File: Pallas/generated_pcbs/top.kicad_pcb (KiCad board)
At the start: 2 copper layers, 467.5 x 140 mm, 17 parts

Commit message: Consolidate symbol and fp libraries
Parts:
- removed the MountBaseMiddleTop15 at (526.4, 136.4)
- removed the MountBaseMiddleTop15 at (526.4, 43.9)
- added MountBaseMiddleTop15: MountingHole, Pallas:MountingHole_2.2mm_M2_Pad_Via, F.Cu at (526.4, 136.4)
- added MountBaseMiddleTop15: MountingHole, Pallas:MountingHole_2.2mm_M2_Pad_Via, F.Cu at (526.4, 43.9)
- LogoBaseMiddleTop: footprint keyboard:Ciaanh_signature -> Pallas:Ciaanh_signature
- MountBaseMiddleTop0, MountBaseMiddleTop10, MountBaseMiddleTop11, MountBaseMiddleTop12, MountBaseMiddleTop13, MountBaseMiddleTop14, MountBaseMiddleTop2, MountBaseMiddleTop3, MountBaseMiddleTop4, MountBaseMiddleTop5, MountBaseMiddleTop6, MountBaseMiddleTop7, MountBaseMiddleTop8, MountBaseMiddleTop9: footprint keyboard:MountingHole_2.2mm_M2_Pad_Via -> Pallas:MountingHole_2.2mm_M2_Pad_Via
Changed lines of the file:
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@@
-(kicad_pcb (version 20171130) (host pcbnew "(5.1.4)-1")
+(kicad_pcb (version 20171130) (host pcbnew 5.1.6-c6e7f7d~86~ubuntu20.04.1)
   (general
     (thickness 1.6)
@@
     (40 Dwgs.User user)
     (41 Cmts.User user)
-    (42 Eco1.User user)
-    (43 Eco2.User user)
+    (42 Eco1.User user hide)
+    (43 Eco2.User user hide)
     (44 Edge.Cuts user)
     (45 Margin user)
@@
       (drillshape 0)
       (scaleselection 1)
-      (outputdirectory "gerber/top/"))
+      (outputdirectory "pallas/"))
   )
   (net 0 "")
@@
     (uvia_drill 0.1)
   )
-  (module keyboard:Ciaanh_signature (layer F.Cu)
+  (module Pallas:Ciaanh_signature (layer F.Cu)
     (at 72.9496 68.7784 270)
     (fp_text reference LogoBaseMiddleTop (at 0.13 6.04 270) (layer F.SilkS) hide
@@
     )
   )
-  (module keyboard:MountingHole_2.2mm_M2_Pad_Via (layer F.Cu)
+  (module Pallas:MountingHole_2.2mm_M2_Pad_Via (layer F.Cu)
     (at 368.8996 48.8784)
     (descr "Mounting Hole 2.2mm, M2")
@@
     (pad 1 thru_hole circle (at 1.166726 -1.166726) (size 0.7 0.7) (drill 0.4) (layers *.Cu *.Mask))
   )
-  (module keyboard:MountingHole_2.2mm_M2_Pad_Via (layer F.Cu)
+  (module Pallas:MountingHole_2.2mm_M2_Pad_Via (layer F.Cu)
     (at 208.8996 48.8784)
     (descr "Mounting Hole 2.2mm, M2")
@@
     (pad 1 thru_hole circle (at 1.166726 -1.166726) (size 0.7 0.7) (drill 0.4) (layers *.Cu *.Mask))
   )
-  (module keyboard:MountingHole_2.2mm_M2_Pad_Via (layer F.Cu)
+  (module Pallas:MountingHole_2.2mm_M2_Pad_Via (layer F.Cu)
     (at 421.3996 136.3784)
     (descr "Mounting Hole 2.2mm, M2")
@@
     (pad 1 thru_hole circle (at 0 0) (size 4.4 4.4) (drill 2.2) (layers *.Cu *.Mask))
   )
-  (module keyboard:MountingHole_2.2mm_M2_Pad_Via (layer F.Cu)
+  (module Pallas:MountingHole_2.2mm_M2_Pad_Via (layer F.Cu)
     (at 121.3996 136.3784)
     (descr "Mounting Hole 2.2mm, M2")
@@
     (pad 1 thru_hole circle (at 0 0) (size 4.4 4.4) (drill 2.2) (layers *.Cu *.Mask))
   )
-  (module keyboard:MountingHole_2.2mm_M2_Pad_Via (layer F.Cu)
+  (module Pallas:MountingHole_2.2mm_M2_Pad_Via (layer F.Cu)
     (at 448.918 80.1114)
     (descr "Mounting Hole 2.2mm, M2")
@@
     (pad 1 thru_hole circle (at 0 0) (size 4.4 4.4) (drill 2.2) (layers *.Cu *.Mask))
   )
-  (module keyboard:MountingHole_2.2mm_M2_Pad_Via (layer F.Cu)
+  (module Pallas:MountingHole_2.2mm_M2_Pad_Via (layer F.Cu)
     (at 128.818 80.1114)
     (descr "Mounting Hole 2.2mm, M2")
@@
     (pad 1 thru_hole circle (at 0 0) (size 4.4 4.4) (drill 2.2) (layers *.Cu *.Mask))
   )
-  (module keyboard:MountingHole_2.2mm_M2_Pad_Via (layer F.Cu)
+  (module Pallas:MountingHole_2.2mm_M2_Pad_Via (layer F.Cu)
     (at 368.8488 92.8784)
     (descr "Mounting Hole 2.2mm, M2")
@@
     (pad 1 thru_hole circle (at 0 0) (size 4.4 4.4) (drill 2.2) (layers *.Cu *.Mask))
   )
-  (module keyboard:MountingHole_2.2mm_M2_Pad_Via (layer F.Cu)
+  (module Pallas:MountingHole_2.2mm_M2_Pad_Via (layer F.Cu)
     (at 208.8488 92.8784)
     (descr "Mounting Hole 2.2mm, M2")
@@
     (pad 1 thru_hole circle (at 0 0) (size 4.4 4.4) (drill 2.2) (layers *.Cu *.Mask))
   )
-  (module keyboard:MountingHole_2.2mm_M2_Pad_Via (layer F.Cu)
+  (module Pallas:MountingHole_2.2mm_M2_Pad_Via (layer F.Cu)
     (at 316.3996 45.8784)
     (descr "Mounting Hole 2.2mm, M2")
@@
     (pad 1 thru_hole circle (at 0 0) (size 4.4 4.4) (drill 2.2) (layers *.Cu *.Mask))
   )
-  (module keyboard:MountingHole_2.2mm_M2_Pad_Via (layer F.Cu)
+  (module Pallas:MountingHole_2.2mm_M2_Pad_Via (layer F.Cu)
     (at 261.3996 45.8784)
     (descr "Mounting Hole 2.2mm, M2")
@@
     (pad 1 thru_hole circle (at 0 0) (size 4.4 4.4) (drill 2.2) (layers *.Cu *.Mask))
   )
-  (module keyboard:MountingHole_2.2mm_M2_Pad_Via (layer F.Cu)
+  (module Pallas:MountingHole_2.2mm_M2_Pad_Via (layer F.Cu)
     (at 248.8488 147.8784)
     (descr "Mounting Hole 2.2mm, M2")
@@
     (pad 1 thru_hole circle (at 0 0) (size 4.4 4.4) (drill 2.2) (layers *.Cu *.Mask))
   )
-  (module keyboard:MountingHole_2.2mm_M2_Pad_Via (layer F.Cu)
+  (module Pallas:MountingHole_2.2mm_M2_Pad_Via (layer F.Cu)
     (at 328.8488 147.8784)
     (descr "Mounting Hole 2.2mm, M2")
@@
     (pad 1 thru_hole circle (at 0 0) (size 4.4 4.4) (drill 2.2) (layers *.Cu *.Mask))
   )
-  (module keyboard:MountingHole_2.2mm_M2_Pad_Via (layer F.Cu)
+  (module Pallas:MountingHole_2.2mm_M2_Pad_Via (layer F.Cu)
     (at 526.3996 136.3784)
     (descr "Mounting Hole 2.2mm, M2")
@@
     (pad 1 thru_hole circle (at 0 0) (size 4.4 4.4) (drill 2.2) (layers *.Cu *.Mask))
   )
-  (module keyboard:MountingHole_2.2mm_M2_Pad_Via (layer F.Cu)
+  (module Pallas:MountingHole_2.2mm_M2_Pad_Via (layer F.Cu)
     (at 526.3996 43.8784)
     (descr "Mounting Hole 2.2mm, M2")
@@
     (pad 1 thru_hole circle (at 0 0) (size 4.4 4.4) (drill 2.2) (layers *.Cu *.Mask))
   )
-  (module keyboard:MountingHole_2.2mm_M2_Pad_Via (layer F.Cu)
+  (module Pallas:MountingHole_2.2mm_M2_Pad_Via (layer F.Cu)
     (at 68.8996 136.3784)
     (descr "Mounting Hole 2.2mm, M2")
@@
     (pad 1 thru_hole circle (at 0 0) (size 4.4 4.4) (drill 2.2) (layers *.Cu *.Mask))
   )
-  (module keyboard:MountingHole_2.2mm_M2_Pad_Via (layer F.Cu)
+  (module Pallas:MountingHole_2.2mm_M2_Pad_Via (layer F.Cu)
     (at 68.8996 43.8784)
     (descr "Mounting Hole 2.2mm, M2")
@@
   (gr_line (start 474.765 101.215) (end 488.735 101.215) (layer Edge.Cuts) (width 0.05))
   (gr_line (start 474.765 115.185) (end 474.765 101.215) (layer Edge.Cuts) (width 0.05))
-  (gr_line (start 337.212718 157.7848) (end 347.091 147.906518) (layer Edge.Cuts) (width 0.05))
-  (gr_line (start 347.091 167.663082) (end 337.212718 157.7848) (layer Edge.Cuts) (width 0.05))
-  (gr_line (start 356.969282 157.7848) (end 347.091 167.663082) (layer Edge.Cuts) (width 0.05))
-  (gr_line (start 347.091 147.906518) (end 356.969282 157.7848) (layer Edge.Cuts) (width 0.05))
   (gr_line (start 432.100576 125.048902) (end 445.765298 122.144376) (layer Edge.Cuts) (width 0.05))
   (gr_line (start 435.005102 138.713624) (end 432.100576 125.048902) (layer Edge.Cuts) (width 0.05))
@@
   (gr_line (start 503.34 82.115) (end 517.325 82.115) (layer Edge.Cuts) (width 0.05))
   (gr_line (start 503.34 105.61) (end 503.34 94.9166) (layer Edge.Cuts) (width 0.05))
+  (gr_line (start 337.212718 157.7848) (end 347.091 147.906518) (layer Edge.Cuts) (width 0.05))
+  (gr_line (start 347.091 167.663082) (end 337.212718 157.7848) (layer Edge.Cuts) (width 0.05))
+  (gr_line (start 356.969282 157.7848) (end 347.091 167.663082) (layer Edge.Cuts) (width 0.05))
+  (gr_line (start 347.091 147.906518) (end 356.969282 157.7848) (layer Edge.Cuts) (width 0.05))
   (gr_line (start 234.3996 49.4784) (end 255.3996 49.4784) (layer Edge.Cuts) (width 0.05))
   (gr_arc (start 255.3996 52.4784) (end 258.3996 52.4784) (angle -90) (layer Edge.Cuts) (width 0.05))

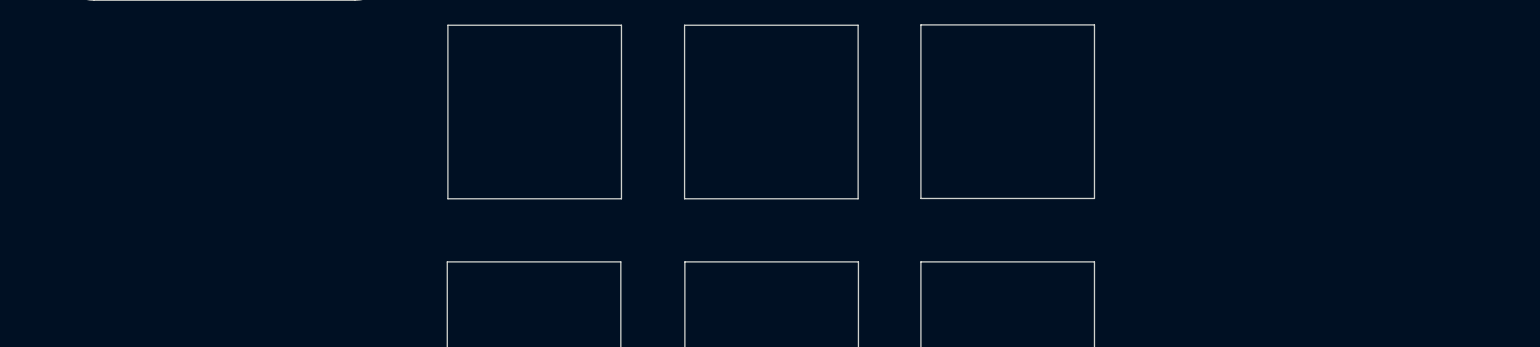
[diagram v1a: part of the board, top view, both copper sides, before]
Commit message: update pcb for footprint stabs
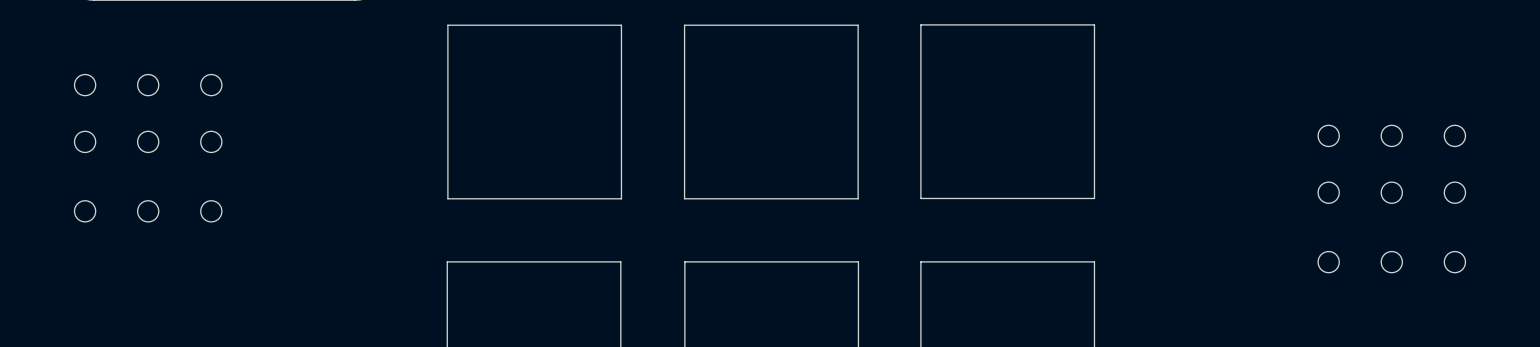
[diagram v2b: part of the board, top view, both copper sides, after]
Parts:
- added DecorationHoleTop1: DecorationHole, Pallas:DecorationHole, F.Cu at (238.7, 96.3)
- added DecorationHoleTop2: DecorationHole, Pallas:DecorationHole, F.Cu at (338.8, 100.4)

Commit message: rev 0.2 fix diode an res position with stabs
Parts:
- DecorationHoleTop2: moved to B.Cu
- moved DecorationHoleTop1 17.7 mm to (238.9, 114.0)
- moved DecorationHoleTop2 13.6 mm to (338.9, 114.0), turned to 180 degrees
